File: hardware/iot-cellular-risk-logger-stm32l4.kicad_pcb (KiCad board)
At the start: 2 copper layers, 54 parts, among them J1 NanoSIM, J2 U.FL Antenna Connector (Male), J3 U.FL Antenna Connector (Male), J4 USB Type-C, J5 Conn_ARM_JTAG_SWD_10, Q1 IRLML6401, Q2 DTC143Z, U1 STM32L433CBUx, U2 SIM7070G, U3 W25Q64JV, U5 SHT30-DIS, U6 MCP73831-2-OT, U7 L78L33ABUTR, U8 TXB0108PWR, U9 SMF05CT1G, Y1 SC-32S32.768

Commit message: schematics: add GSM, USART, level shifter, SIM nets&labels
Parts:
- removed U9: SMF05CT1G, Package_TO_SOT_SMD:SOT-363_SC-70-6
- added C23: 100n, Capacitor_SMD:C_0603_1608Metric_Pad1.08x0.95mm_HandSolder, F.Cu at (107.3, 60.2)
- added D3: BZT52C4V7, Diode_SMD:D_SOD-123F, F.Cu at (135.2, 27.8)
- added D4: SMF05CT1G, Package_TO_SOT_SMD:SOT-23-6, F.Cu at (94.7, 60.2)
- BT1: value Battery_Cell -> 18650 LiFePO4
- J1: value NanoSIM -> Nano SIM; footprint personal:MOLEX_104224-0820 -> personal:GCT_SIM8066-6-1-14-01-A_REVA
- moved J1 12.7 mm to (124.3, 32.8)
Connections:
- C13 pad 2: unconnected-(C13-Pad2) -> GND
- C14 pad 2: unconnected-(C14-Pad2) -> GND
- C15 pad 2: unconnected-(C15-Pad2) -> GND
- C16 pad 2: unconnected-(C16-Pad2) -> GND
- C17 pad 2: unconnected-(C17-Pad2) -> GND
- J1 pad G1: Net-(J1-GND-PadG1) -> GND
- J1 pad G2: Net-(J1-GND-PadG1) -> GND
- J1 pad G3: Net-(J1-GND-PadG1) -> GND
- J1 pad G4: Net-(J1-GND-PadG1) -> GND
- J2 pad 3: unconnected-(J2-SIG-Pad3) -> GSM_RF
- J3 pad 3: unconnected-(J3-SIG-Pad3) -> GPS_RF
- Q2 pad 1: PWRKEY -> GSM_PWR
- Q2 pad 3: Net-(Q2-C) -> PWRKEY
- U2 pad 1: Net-(Q2-C) -> PWRKEY
- U2 pad 10: unconnected-(U2-UART1_RXD-Pad10) -> /RX
- U2 pad 3: unconnected-(U2-UART1_DTR-Pad3) -> /DTR
- U2 pad 30: unconnected-(U2-SIM_VDD-Pad30) -> /VDD
- U2 pad 31: unconnected-(U2-SIM_DATA-Pad31) -> /DATA
- U2 pad 32: unconnected-(U2-SIM_CLK-Pad32) -> /CLK
- U2 pad 33: unconnected-(U2-SIM_RST-Pad33) -> /RST
- U2 pad 4: unconnected-(U2-UART1_RI-Pad4) -> /RI
- U2 pad 5: unconnected-(U2-UART1_DCD-Pad5) -> /DCD
- U2 pad 53: unconnected-(U2-GNSS_ANT-Pad53) -> GPS_RF
- U2 pad 60: unconnected-(U2-RF_ANT-Pad60) -> GSM_RF
- U2 pad 7: unconnected-(U2-UART1_CTS-Pad7) -> /CTS
- U2 pad 8: unconnected-(U2-UART1_RTS-Pad8) -> /RTS
- U2 pad 9: unconnected-(U2-UART1_TXD-Pad9) -> /TX
- U8 pad 1: unconnected-(U8-A1-Pad1) -> /RX
- U8 pad 2: unconnected-(U8-A2-Pad2) -> /TX
- U8 pad 3: unconnected-(U8-A3-Pad3) -> /RTS
- U8 pad 4: unconnected-(U8-A4-Pad4) -> /CTS
- U8 pad 7: unconnected-(U8-A5-Pad7) -> /DCD
- U8 pad 8: unconnected-(U8-A6-Pad8) -> /RI
- U8 pad 9: unconnected-(U8-A7-Pad9) -> /DTR

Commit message: schematics: add QSPI, rework PMU, add sim, gsm, shifter nets
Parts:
- added AE1: GNSS Ceramic Antenna 25x25x4, personal:XDCR_APAE1590R2540AKDB1-T, F.Cu at (177.0, 48.0)
- C6: value 1u -> 100n; footprint Capacitor_SMD:C_0805_2012Metric_Pad1.18x1.45mm_HandSolder -> Capacitor_SMD:C_0603_1608Metric_Pad1.08x0.95mm_HandSolder
- J5: value Conn_ARM_JTAG_SWD_10 -> TagConnect SWD ARM
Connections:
- net /VBAT renamed /GSM_VBAT
- C10 pad 1: Net-(C10-Pad1) -> /LSE IN
- C11 pad 1: Net-(C11-Pad1) -> /LSE OUT
- C5 pad 1: /VDDA -> /MCU_VDD
- C6 pad 1: /VDDA -> /MCU_VDD
- C7 pad 1: +3V3 -> /MCU_VDD
- C8 pad 1: +3V3 -> /MCU_VDD
- C9 pad 1: +3V3 -> /MCU_VDD
- FB1 pad 2: /VDDA -> /MCU_VDD
- J2 pad 1: Net-(J2-GND-Pad1) -> GND
- J2 pad 2: Net-(J2-GND-Pad1) -> GND
- J3 pad 1: Net-(J3-GND-Pad1) -> GND
- J3 pad 2: Net-(J3-GND-Pad1) -> GND
- J5 pad 1: +3V0 -> +3V3
- U1 pad 23: Net-(U1-VSS-Pad23) -> GND
- U1 pad 24: unconnected-(U1-VDD-Pad24) -> /MCU_VDD
- U1 pad 27: unconnected-(U1-PB14-Pad27) -> /CTS3V
- U1 pad 28: unconnected-(U1-PB15-Pad28) -> /CTS3V
- U1 pad 29: unconnected-(U1-PA8-Pad29) -> /CTS3V
- U1 pad 3: unconnected-(U1-PC14-Pad3) -> /LSE IN
- U1 pad 30: unconnected-(U1-PA9-Pad30) -> /CTS3V
- U1 pad 31: unconnected-(U1-PA10-Pad31) -> /CTS3V
- U1 pad 32: unconnected-(U1-PA11-Pad32) -> /CTS3V
- U1 pad 33: unconnected-(U1-PA12-Pad33) -> /CTS3V
- U1 pad 34: unconnected-(U1-PA13-Pad34) -> SWDIO
- U1 pad 35: Net-(U1-VSS-Pad23) -> GND
- U1 pad 36: unconnected-(U1-VDDUSB-Pad36) -> /MCU_VDD
- U1 pad 37: unconnected-(U1-PA14-Pad37) -> SWDCLK
- U1 pad 39: unconnected-(U1-PB3-Pad39) -> SWO
- U1 pad 4: unconnected-(U1-PC15-Pad4) -> /LSE OUT
- U1 pad 47: Net-(U1-VSS-Pad23) -> GND
- U1 pad 48: unconnected-(U1-VDD-Pad48) -> /MCU_VDD
- U1 pad 49: Net-(U1-VSS-Pad23) -> GND
- U1 pad 7: unconnected-(U1-NRST-Pad7) -> _RESET
- U1 pad 8: unconnected-(U1-VSSA-Pad8) -> GND
- U1 pad 9: unconnected-(U1-VDDA-Pad9) -> /MCU_VDD
- U2 pad 17: Net-(U2-GND-Pad17) -> GND
- U2 pad 18: Net-(U2-GND-Pad17) -> GND
- U2 pad 2: Net-(U2-GND-Pad17) -> GND
- U2 pad 29: Net-(U2-GND-Pad17) -> GND
- U2 pad 39: Net-(U2-GND-Pad17) -> GND
- U2 pad 45: Net-(U2-GND-Pad17) -> GND
- U2 pad 46: Net-(U2-GND-Pad17) -> GND
- U2 pad 54: Net-(U2-GND-Pad17) -> GND
- U2 pad 58: Net-(U2-GND-Pad17) -> GND
- U2 pad 59: Net-(U2-GND-Pad17) -> GND
- U2 pad 61: Net-(U2-GND-Pad17) -> GND
- U2 pad 62: Net-(U2-GND-Pad17) -> GND
- U2 pad 63: Net-(U2-GND-Pad17) -> GND
- U2 pad 64: Net-(U2-GND-Pad17) -> GND
- U2 pad 65: Net-(U2-GND-Pad17) -> GND
- U8 pad 12: unconnected-(U8-B7-Pad12) -> /CTS3V
- U8 pad 13: unconnected-(U8-B6-Pad13) -> /CTS3V
- U8 pad 14: unconnected-(U8-B5-Pad14) -> /CTS3V
- U8 pad 17: unconnected-(U8-B4-Pad17) -> /CTS3V
- U8 pad 18: unconnected-(U8-B3-Pad18) -> /CTS3V
- U8 pad 19: unconnected-(U8-B2-Pad19) -> /CTS3V
- U8 pad 20: unconnected-(U8-B1-Pad20) -> /CTS3V
- Y1 pad 1: Net-(C10-Pad1) -> /LSE IN
- Y1 pad 2: Net-(C11-Pad1) -> /LSE OUT

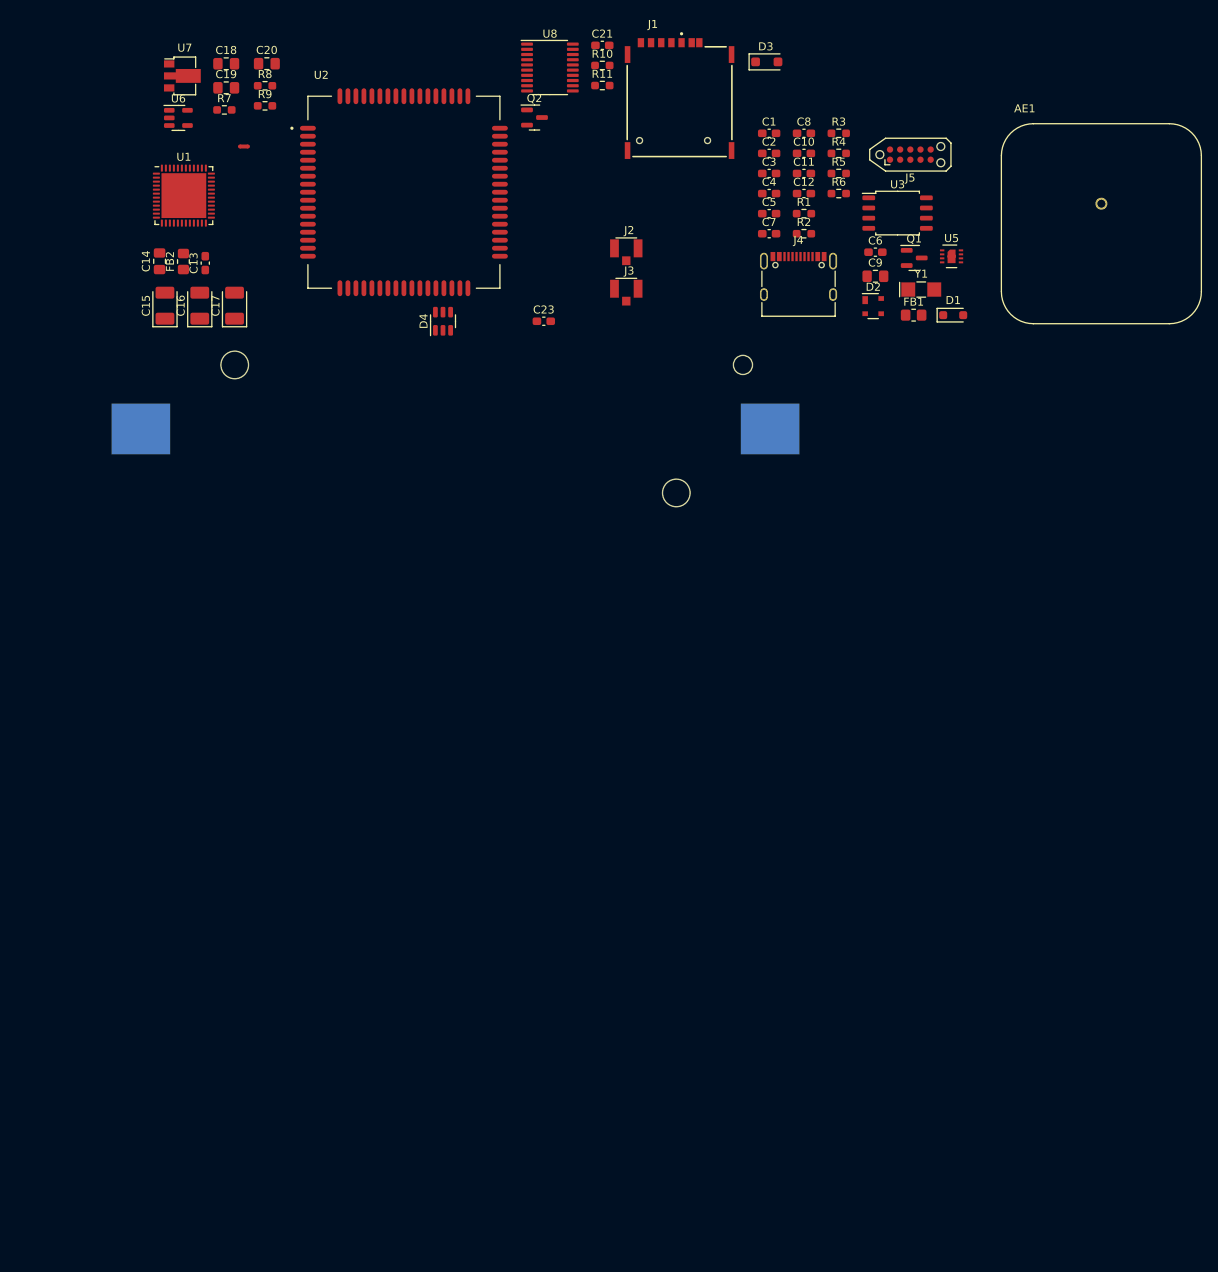
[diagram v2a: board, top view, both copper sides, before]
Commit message: PCB: manual RF routes done
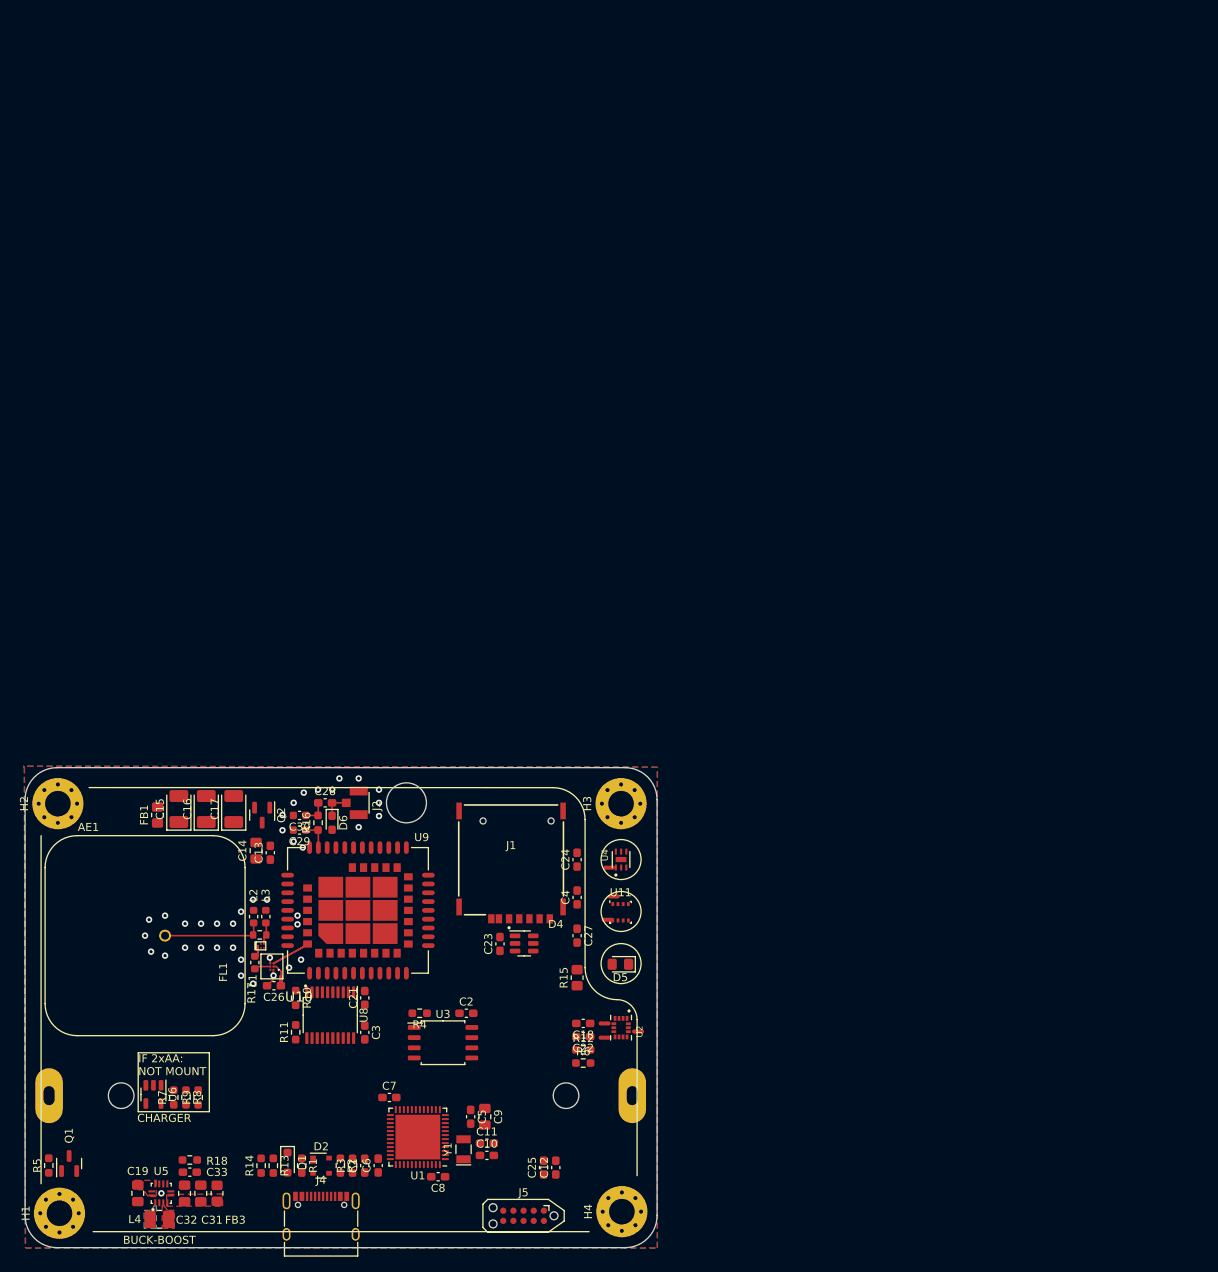
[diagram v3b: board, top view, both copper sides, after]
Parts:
- removed C20: 10u, Capacitor_SMD:C_0805_2012Metric_Pad1.18x1.45mm_HandSolder
- removed D3: BZT52C4V7, Diode_SMD:D_SOD-123F
- removed FB2: 330, Resistor_SMD:R_0805_2012Metric_Pad1.20x1.40mm_HandSolder
- removed J3: U.FL Antenna Connector (Male), personal:HRS_U.FL-R-SMT_01_
- removed U7: L78L33ABUTR, Package_TO_SOT_SMD:SOT-89-3
- added C22: 100n, Capacitor_SMD:C_0603_1608Metric_Pad1.08x0.95mm_HandSolder, F.Cu at (112.3, 149.6)
- added C24: 100n, Capacitor_SMD:C_0603_1608Metric_Pad1.08x0.95mm_HandSolder, F.Cu at (111.5, 127.5)
- added C25: 100n, Capacitor_SMD:C_0603_1608Metric_Pad1.08x0.95mm_HandSolder, F.Cu at (107.3, 166.0)
- added C26: 100n, Capacitor_SMD:C_0603_1608Metric_Pad1.08x0.95mm_HandSolder, F.Cu at (73.6, 143.3)
- added C27: 100n, Capacitor_SMD:C_0603_1608Metric_Pad1.08x0.95mm_HandSolder, F.Cu at (111.5, 137.0)
- added C28: 100p, Capacitor_SMD:C_0603_1608Metric_Pad1.08x0.95mm_HandSolder, F.Cu at (80.0, 120.4)
- added C29: 0p, Capacitor_SMD:C_0603_1608Metric, F.Cu at (76.8, 123.8)
- added C30: 0p, Capacitor_SMD:C_0603_1608Metric, F.Cu at (76.8, 122.0)
- added C31: 10u, Capacitor_SMD:C_0805_2012Metric_Pad1.18x1.45mm_HandSolder, F.Cu at (64.5, 169.2)
- added C32: 10u, Capacitor_SMD:C_0805_2012Metric_Pad1.18x1.45mm_HandSolder, F.Cu at (62.4, 169.2)
- added C33: 1n, Capacitor_SMD:C_0603_1608Metric_Pad1.08x0.95mm_HandSolder, F.Cu at (63.1, 166.6)
- added D5: LED, LED_SMD:LED_0805_2012Metric_Pad1.15x1.40mm_HandSolder, F.Cu at (116.9, 140.6)
- added D6: TVS 5V, Diode_SMD:D_0603_1608Metric_Pad1.05x0.95mm_HandSolder, F.Cu at (80.9, 122.9)
- added FB3: 330, Resistor_SMD:R_0805_2012Metric_Pad1.20x1.40mm_HandSolder, F.Cu at (66.5, 169.2)
- added FL1: SAFFB1G56KB0F0A, Filter:Filter_1109-5_1.1x0.9mm, F.Cu at (72.0, 138.3)
- added H1: MountingHole_Pad, MountingHole:MountingHole_3.2mm_M3_Pad_Via, F.Cu at (46.8, 171.7)
- added H2: MountingHole_Pad, MountingHole:MountingHole_3.2mm_M3_Pad_Via, F.Cu at (46.6, 120.5)
- added H3: MountingHole_Pad, MountingHole:MountingHole_3.2mm_M3_Pad_Via, F.Cu at (117.0, 120.5)
- added H4: MountingHole_Pad, MountingHole:MountingHole_3.2mm_M3_Pad_Via, F.Cu at (117.1, 171.5)
- added L1: 8.2nH, Inductor_SMD:L_0603_1608Metric, F.Cu at (71.2, 140.4)
- added L2: 0L, Inductor_SMD:L_0603_1608Metric, F.Cu at (71.1, 134.6)
- added L3: 0L, Inductor_SMD:L_0603_1608Metric, F.Cu at (72.6, 134.6)
- added L4: 1.5uH, Inductor_SMD:L_1008_2520Metric_Pad1.43x2.20mm_HandSolder, F.Cu at (59.3, 172.5)
- added NT2: NetTie_2, NetTie:NetTie-2_SMD_Pad0.5mm, F.Cu at (114.9, 148.0)
- added NT3: NetTie_2, NetTie:NetTie-2_SMD_Pad0.5mm, F.Cu at (116.1, 132.1)
- added NT4: NetTie_2, NetTie:NetTie-2_SMD_Pad0.5mm, F.Cu at (115.5, 128.5)
- added NT5: NetTie_2, NetTie:NetTie-2_SMD_Pad0.5mm, F.Cu at (119.1, 149.0)
- added NT6: NetTie_2, NetTie:NetTie-2_SMD_Pad0.5mm, F.Cu at (74.5, 142.6)
- added NT7: NetTie_2, NetTie:NetTie-2_SMD_Pad0.5mm, F.Cu at (115.3, 135.0)
- added R12: 4k7, Resistor_SMD:R_0603_1608Metric_Pad0.98x0.95mm_HandSolder, F.Cu at (112.3, 151.3)
- added R13: 47k, Resistor_SMD:R_0603_1608Metric_Pad0.98x0.95mm_HandSolder, F.Cu at (73.5, 165.7)
- added R14: 47k, Resistor_SMD:R_0603_1608Metric_Pad0.98x0.95mm_HandSolder, F.Cu at (72.0, 165.7)
- added R15: 1k, Resistor_SMD:R_0805_2012Metric_Pad1.20x1.40mm_HandSolder, F.Cu at (111.5, 142.3)
- added R16: 0R, Resistor_SMD:R_0603_1608Metric_Pad0.98x0.95mm_HandSolder, F.Cu at (79.1, 122.9)
- added R17: 0R, Resistor_SMD:R_0603_1608Metric, F.Cu at (71.8, 136.9)
- added R18: 1M, Resistor_SMD:R_0603_1608Metric_Pad0.98x0.95mm_HandSolder, F.Cu at (63.1, 165.0)
- added U10: BGA 524N6 E6327, personal:BGA524N6E6327, F.Cu at (73.4, 140.9)
- added U11: BME280, Package_LGA:Bosch_LGA-8_2.5x2.5mm_P0.65mm_ClockwisePinNumbering, F.Cu at (116.9, 134.1)
- added U4: OPT3001DNPR, personal:SON65P200X200X65-7N, F.Cu at (117.0, 127.5)
- added U9: SIM7080G, personal:XCVR_SIM7080G, F.Cu at (84.1, 133.8)
- AE1: value GNSS Ceramic Antenna 25x25x4 -> GNSS Antenna
- BT1: value 18650 LiFePO4 -> 18650 Li-Ion; footprint Battery:BatteryHolder_Keystone_1042_1x18650 -> personal:BAT_BH-18650-PC
- C18: value 10u -> 100n; footprint Capacitor_SMD:C_0805_2012Metric_Pad1.18x1.45mm_HandSolder -> Capacitor_SMD:C_0603_1608Metric_Pad1.08x0.95mm_HandSolder
- R5: value 47k -> 100k
- R6: value 47k -> 4k7
- R7: value 5k1 -> 2k5
- U2: value SIM7070G -> LSM6DSO; footprint personal:MODULE_SIM7070G -> personal:PQFN50P250X300X86-14N
- U5: value SHT30-DIS -> TPS63051; footprint Sensor_Humidity:Sensirion_DFN-8-1EP_2.5x2.5mm_P0.5mm_EP1.1x1.7mm -> personal:QFN50P250X250X100-12N
- Y1: footprint Crystal:Crystal_SMD_EuroQuartz_EQ161-2Pin_3.2x1.5mm_HandSoldering -> Crystal:Crystal_SMD_EuroQuartz_EQ161-2Pin_3.2x1.5mm
- moved R5 158.5 mm to (45.5, 165.7), turned to 90 degrees
- moved Q1 154.8 mm to (48.0, 165.5), turned to 90 degrees
- moved U5 153.2 mm to (59.5, 169.2), turned to 90 degrees
- moved AE1 149.0 mm to (57.5, 137.0), turned to -90 degrees
- moved R3 142.6 mm to (83.4, 165.7), turned to 90 degrees
- moved J5 141.2 mm to (104.8, 172.0), turned to 180 degrees
- moved C19 138.6 mm to (56.6, 169.2), turned to -90 degrees
- moved C1 138.6 mm to (85.0, 165.7), turned to 90 degrees
- moved C8 138.2 mm to (94.1, 167.1), turned to 180 degrees
- moved D1 134.7 mm to (75.3, 165.4), turned to -90 degrees
- moved R1 134.5 mm to (77.1, 165.7), turned to -90 degrees
- moved J4 131.8 mm to (79.5, 173.3)
- moved C10 131.4 mm to (100.2, 164.5)
- moved R2 130.1 mm to (81.9, 165.7), turned to -90 degrees
- moved C6 130.0 mm to (86.6, 165.7), turned to 90 degrees
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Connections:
- net Net-(D1-A) renamed /+VBUS
- net Net-(D2-GND) renamed /GND_SHIELD
- net Net-(J4-CC1) renamed /USB_CC1
- net Net-(J4-CC2) renamed /USB_CC2
- AE1 pad 1: unconnected-(AE1-A-Pad1) -> /GNSS_ANT_RF
- C13 pad 1: /GSM_VBAT -> /+GSM_VBAT
- C14 pad 1: /GSM_VBAT -> /+GSM_VBAT
- C15 pad 1: /GSM_VBAT -> /+GSM_VBAT
- C16 pad 1: /GSM_VBAT -> /+GSM_VBAT
- C17 pad 1: /GSM_VBAT -> /+GSM_VBAT
- C18 pad 1: /BATTERY -> +3V3
- C19 pad 1: +5V -> +BATT
- C2 pad 1: +3V0 -> +3V3
- C4 pad 1: +3V0 -> +3V3
- C5 pad 1: /MCU_VDD -> +3V3
- C6 pad 1: /MCU_VDD -> +3V3
- C7 pad 1: /MCU_VDD -> +3V3
- C8 pad 1: /MCU_VDD -> +3V3
- C9 pad 1: /MCU_VDD -> +3V3
- FB1 pad 1: +3V3 -> /+GSM_VBAT
- FB1 pad 2: /MCU_VDD -> +BATT
- J2 pad 3: GSM_RF -> /GSM_ANT_RF
- NT1 pad 1: +5V -> Net-(U2-VDD)
- NT1 pad 2: +BATT -> +3V3
- Q1 pad 1: +5V -> Net-(Q1-G)
- Q1 pad 3: /BATTERY -> /+BATTERY
- Q2 pad 1: GSM_PWR -> GSM_EN
- Q2 pad 3: PWRKEY -> Net-(Q2-C)
- R4 pad 1: +3V0 -> +3V3
- R4 pad 2: _QSPI_NCS -> /_QSPI_NCS
- R5 pad 1: +5V -> Net-(Q1-G)
- R5 pad 2: USB_VBUS_SENSE -> GND
- R6 pad 1: USB_VBUS_SENSE -> +3V3
- R6 pad 2: GND -> SDA
- U1 pad 10: unconnected-(U1-PA0-Pad10) -> GSM_EN
- U1 pad 11: unconnected-(U1-PA1-Pad11) -> GNSS_EN
- U1 pad 12: unconnected-(U1-PA2-Pad12) -> /_QSPI_NCS
- U1 pad 13: unconnected-(U1-PA3-Pad13) -> /QSPI_CLK
- U1 pad 16: unconnected-(U1-PA6-Pad16) -> /QSPI_IO3
- U1 pad 17: unconnected-(U1-PA7-Pad17) -> /QSPI_IO2
- U1 pad 18: unconnected-(U1-PB0-Pad18) -> /QSPI_IO1
- U1 pad 19: unconnected-(U1-PB1-Pad19) -> /QSPI_IO0
- U1 pad 20: unconnected-(U1-PB2-Pad20) -> SIM_DETECT
- U1 pad 21: unconnected-(U1-PB10-Pad21) -> /RX3V
- U1 pad 22: unconnected-(U1-PB11-Pad22) -> /TX3V
- U1 pad 24: /MCU_VDD -> +3V3
- U1 pad 25: unconnected-(U1-PB12-Pad25) -> /RTS3V
- U1 pad 26: unconnected-(U1-PB13-Pad26) -> /CTS3V
- U1 pad 27: /CTS3V -> /RI3V
- U1 pad 28: /CTS3V -> /DTR3V
- U1 pad 29: /CTS3V -> /DCD3V
- U1 pad 30: /CTS3V -> SCL
- U1 pad 31: /CTS3V -> SDA
- U1 pad 32: /CTS3V -> USB_N
- U1 pad 33: /CTS3V -> USB_P
- U1 pad 36: /MCU_VDD -> +3V3
- U1 pad 38: unconnected-(U1-PA15-Pad38) -> USB_VBUS
- U1 pad 40: unconnected-(U1-PB4-Pad40) -> CHARGE_STAT
- U1 pad 41: unconnected-(U1-PB5-Pad41) -> _LIGHT_INT
- U1 pad 42: unconnected-(U1-PB6-Pad42) -> IMU_INT1
- U1 pad 43: unconnected-(U1-PB7-Pad43) -> IMU_INT2
- U1 pad 48: /MCU_VDD -> +3V3
- U1 pad 9: /MCU_VDD -> +3V3
- U2 pad 1: PWRKEY -> GND
- U2 pad 10: /RX -> unconnected-(U2-OCS_AUX-Pad10)
- U2 pad 12: unconnected-(U2-PCM_SYNC-Pad12) -> Net-(U2-CS)
- U2 pad 13: unconnected-(U2-PCM_DIN-Pad13) -> SCL
- U2 pad 14: unconnected-(U2-PCM_DOUT-Pad14) -> SDA
- U2 pad 3: /DTR -> GND
- U2 pad 4: /RI -> IMU_INT1
- U2 pad 5: /DCD -> Net-(U2-VDDIO)
- U2 pad 6: unconnected-(U2-BOOT_CFG-Pad6) -> GND
- U2 pad 7: /CTS -> GND
- U2 pad 8: /RTS -> Net-(U2-VDD)
- U2 pad 9: /TX -> IMU_INT2
- U3 pad 1: _QSPI_NCS -> /_QSPI_NCS
- U3 pad 2: QSPI_IO1 -> /QSPI_IO1
- U3 pad 3: QSPI_IO2 -> /QSPI_IO2
- U3 pad 5: QSPI_IO0 -> /QSPI_IO0
- U3 pad 6: QSPI_CLK -> /QSPI_CLK
- U3 pad 7: QSPI_IO3 -> /QSPI_IO3
- U3 pad 8: +3V0 -> +3V3
- U5 pad 1: SDA -> /IND1
- U5 pad 3: TEMP_INT -> /IND2
- U5 pad 4: SCL -> /+VOUT
- U5 pad 5: +3V0 -> /+VOUT
- U5 pad 6: _TEMP_RESET -> GND
- U5 pad 7: GND -> Net-(U5-SS)
- U5 pad 8: GND -> Net-(U5-PG)
- U6 pad 3: /BATTERY -> +BATT
- U8 pad 1: /RX -> /RI
- U8 pad 12: /CTS3V -> /RX3V
- U8 pad 13: /CTS3V -> /TX3V
- U8 pad 14: /CTS3V -> /RTS3V
- U8 pad 18: /CTS3V -> /DCD3V
- U8 pad 19: /CTS3V -> /DTR3V
- U8 pad 2: /TX -> /DTR
- U8 pad 20: /CTS3V -> /RI3V
- U8 pad 3: /RTS -> /DCD
- U8 pad 7: /DCD -> /RTS
- U8 pad 8: /RI -> /RX
- U8 pad 9: /DTR -> /TX
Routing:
- net /GNSS_ANT_RF: track 0.00 -> 12.7 mm
- net GNSS_RF: track 0.00 -> 4.52 mm
- net GSM_RF: track 0.00 -> 3.92 mm
- net /GSM_ANT_RF: track 0.00 -> 3.34 mm
- net /GNSS_M_RF: track 0.00 -> 3.20 mm
- net /GSM_M_RF: track 0.00 -> 3.17 mm
- net GND: track 0.00 -> 3.07 mm, vias 0 -> 38
- net /VCC_LNA: track 0.00 -> 1.87 mm
- net /LNA_RF: track 0.00 -> 1.64 mm
- net /SAW_RF: track 0.00 -> 1.17 mm
- net Net-(Q2-C): vias 0 -> 1
- net +1V8: vias 0 -> 1
- added copper zone on F.Cu, net +BATT
- added copper zone on F.Cu, net /+VOUT
- added copper zone on B.Cu, net /IND1
- added copper zone on F.Cu, net /IND2
- added copper zone on B.Cu, net GND
- added copper zone on F.Cu, net GND
- added copper zone on In1.Cu, net GND
- added copper zone on In2.Cu, net GND
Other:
- board outline added: 79 x 60 mm
- copper layers 2 -> 4
- board text added: "BUCK-BOOST"
- board text added: "CHARGER"
- board text added: "IF 2xAA: NOT MOUNT"
